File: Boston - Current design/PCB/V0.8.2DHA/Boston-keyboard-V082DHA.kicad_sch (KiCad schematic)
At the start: 320 parts, among them J701 Conn_01x04_MountingPin, J702 Conn_01x03, J705 Conn_01x04_MountingPin, J706 Conn_ARM_JTAG_SWD_10, Q701 DTC123J, SW1 MXSwitch, SW10 MXSwitch, SW100 MXSwitch, SW101 MXSwitch, SW102 MXSwitch, SW103 MXSwitch, SW104 MXSwitch, SW105-1 MXSwitch, SW105-2 MXSwitch, SW106 MXSwitch, SW107 MXSwitch, SW108 MXSwitch, SW109 MXSwitch, SW11 MXSwitch, SW110 MXSwitch, SW111 MXSwitch, SW112 MXSwitch, SW113 MXSwitch, SW114 MXSwitch, SW115 MXSwitch, SW116 MXSwitch, SW117 MXSwitch, SW118 MXSwitch, SW119 MXSwitch, SW120 MXSwitch, SW121 MXSwitch, SW122 MXSwitch, SW123 MXSwitch, SW124-1 MXSwitch, SW124-2 MXSwitch, SW125 MXSwitch, SW126 Rotary_Encoder_Switch_Chassis, SW127 MXSwitch, SW128 MXSwitch, SW129 MXSwitch, SW13 MXSwitch, SW14 MXSwitch, SW15 MXSwitch, SW16 MXSwitch, SW17 MXSwitch, SW18 MXSwitch, SW19 MXSwitch, SW2 MXSwitch, SW20 MXSwitch, SW200 SW_Push, SW21 MXSwitch, SW22 MXSwitch, SW23 MXSwitch, SW24 MXSwitch, SW25 MXSwitch, SW26 MXSwitch, SW27 MXSwitch, SW28 MXSwitch, SW29 MXSwitch, SW3 MXSwitch, SW30 MXSwitch, SW31 MXSwitch, SW32 MXSwitch, SW33 MXSwitch, SW34 MXSwitch, SW35 MXSwitch, SW36 MXSwitch, SW37 MXSwitch, SW38 MXSwitch, SW39-1 MXSwitch, SW39-2 MXSwitch, SW4 MXSwitch, SW40 MXSwitch, SW41 MXSwitch, SW42 MXSwitch, SW43 MXSwitch, SW44 MXSwitch, SW45 MXSwitch, SW46 MXSwitch, SW47 MXSwitch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

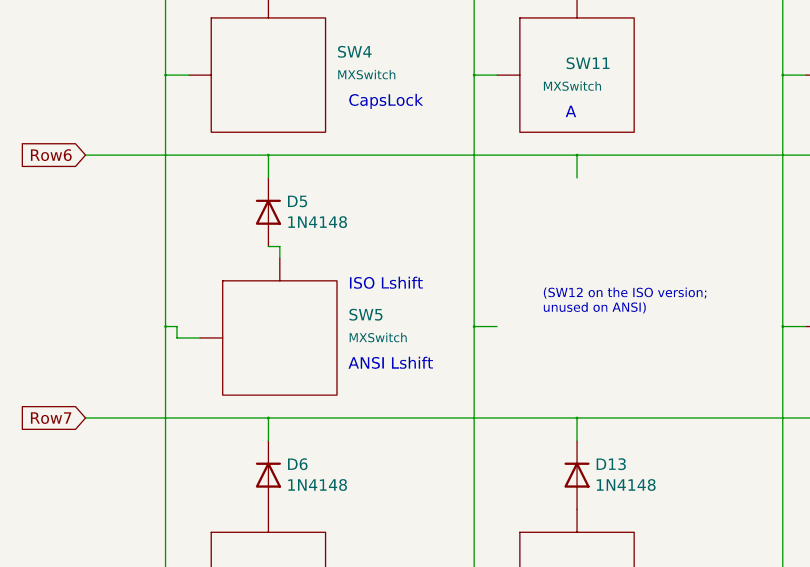
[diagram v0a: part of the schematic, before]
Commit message: Removed unused ISO left shift reference in the schematic
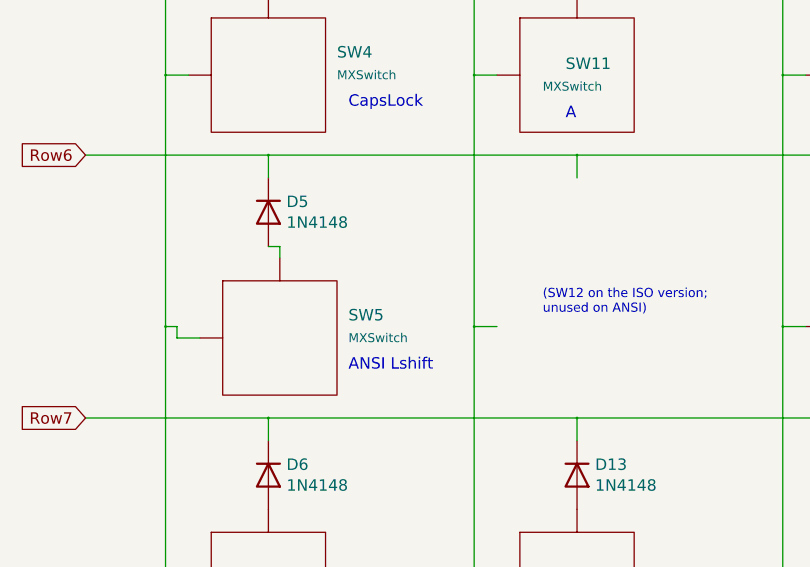
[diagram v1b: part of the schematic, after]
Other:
- note removed: "ISO Lshift"
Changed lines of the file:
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@@
-    (effects (font (size 1.27 1.27)) (justify left bottom))
-  )
-  (text "ISO Lshift\n" (at 54.61 200.66 0)
     (effects (font (size 1.27 1.27)) (justify left bottom))
   )

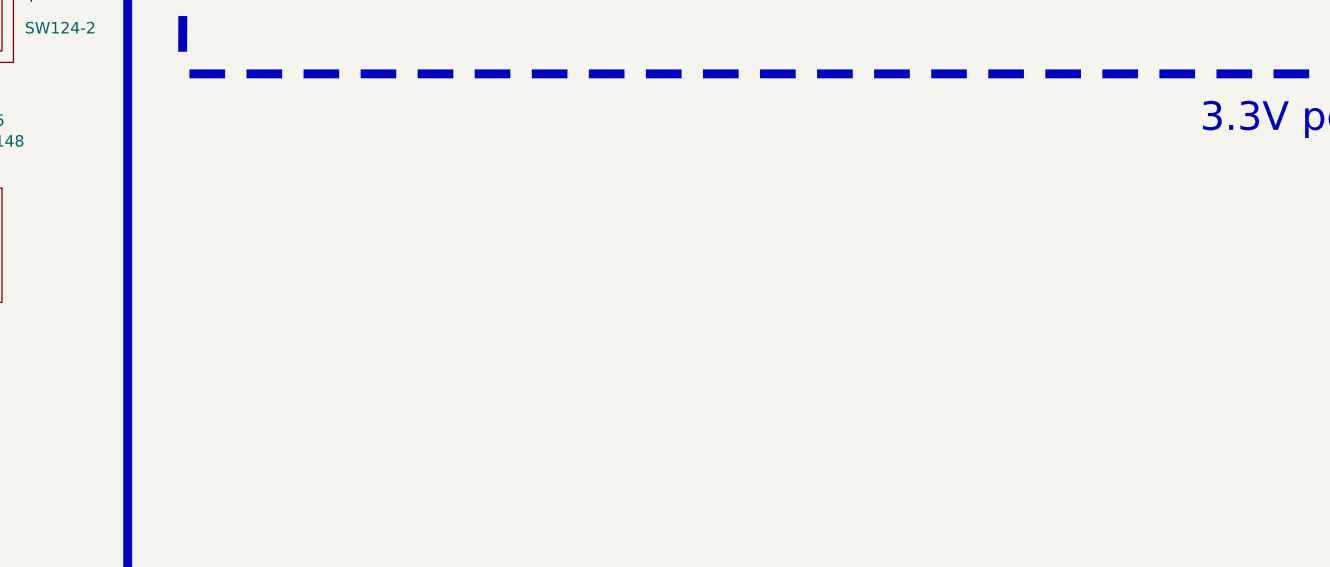
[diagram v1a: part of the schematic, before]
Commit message: Added note that SW123 and SW124-2 were accidentally swapped in the PCB layout
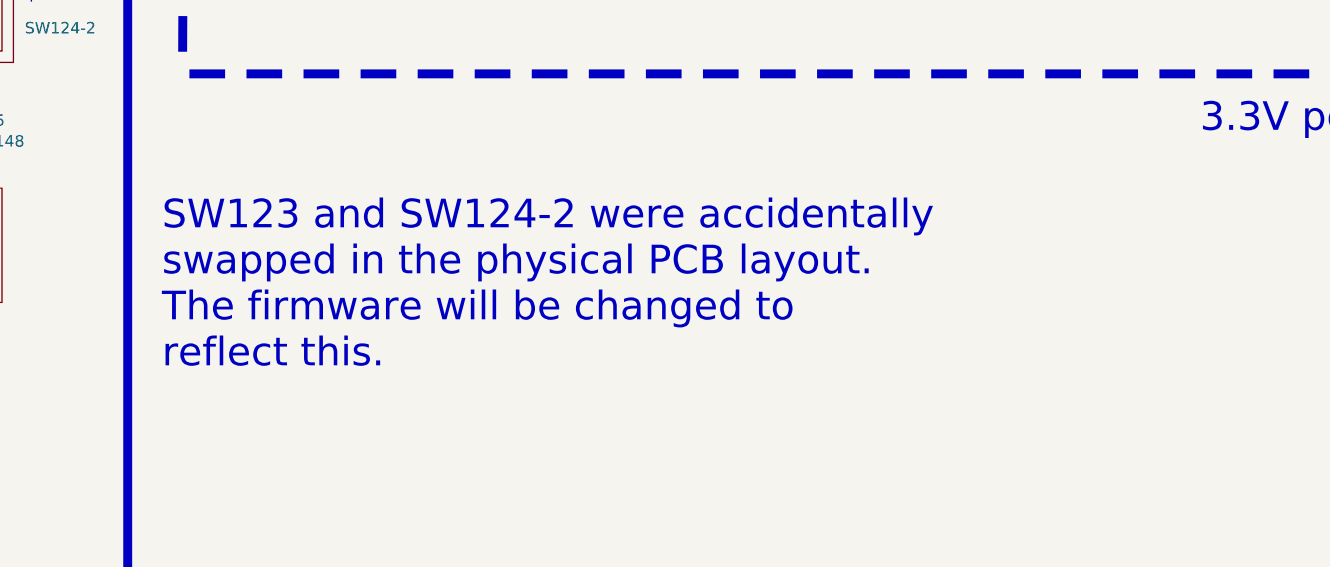
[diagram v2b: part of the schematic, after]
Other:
- note added: "SW123 and SW124-2 were accidentally swapped in the physical PCB layout. The firmware will be changed to reflect this."
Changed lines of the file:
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@@
     (effects (font (size 1.27 1.27)) (justify left bottom))
+  )
+  (text "SW123 and SW124-2 were accidentally \nswapped in the physical PCB layout. \nThe firmware will be changed to \nreflect this."
+    (at 694.69 218.44 0)
+    (effects (font (size 3.175 3.175)) (justify left bottom))
   )
   (text "I" (at 318.77 153.67 0)
